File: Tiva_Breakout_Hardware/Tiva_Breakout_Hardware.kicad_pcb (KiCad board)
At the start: 2 copper layers, 139.8 x 79.5 mm, 11 parts, among them U1 TM4C129E_Launchpad

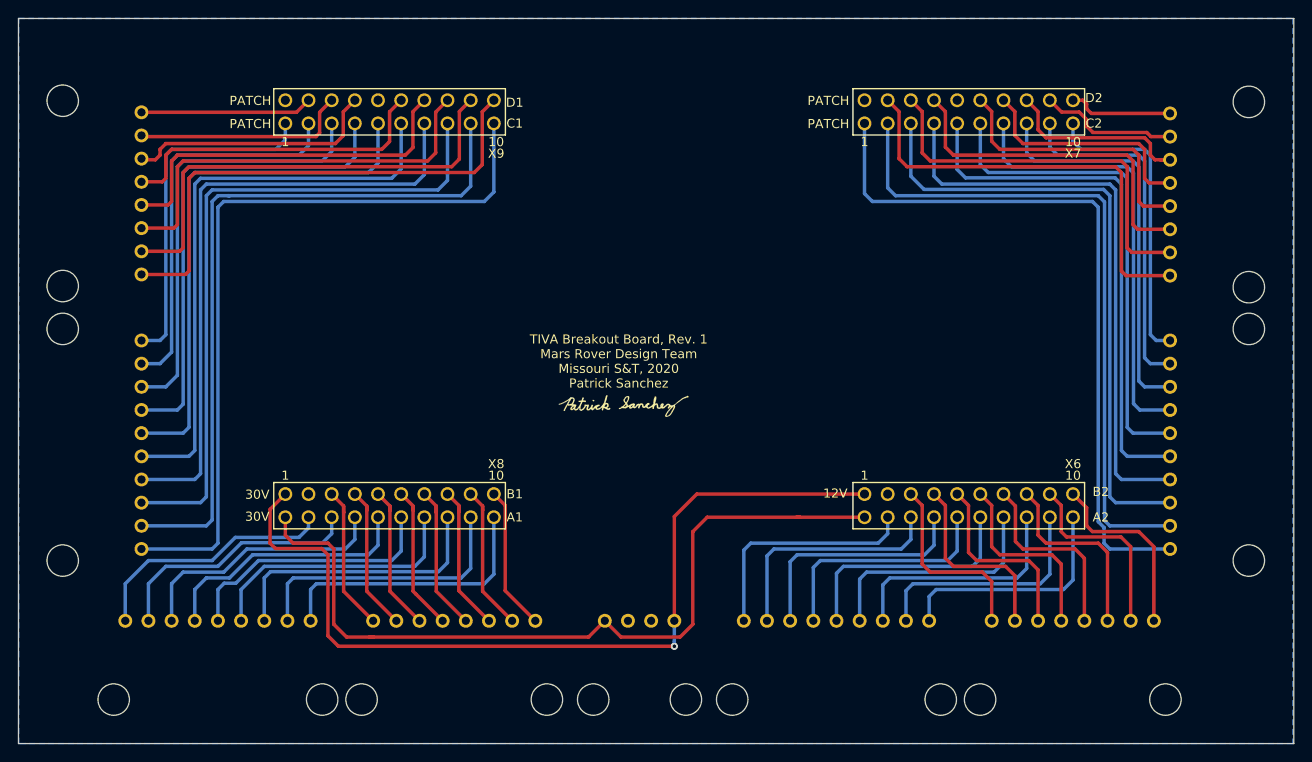
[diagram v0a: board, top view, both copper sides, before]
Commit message: renamed board folder to match standards
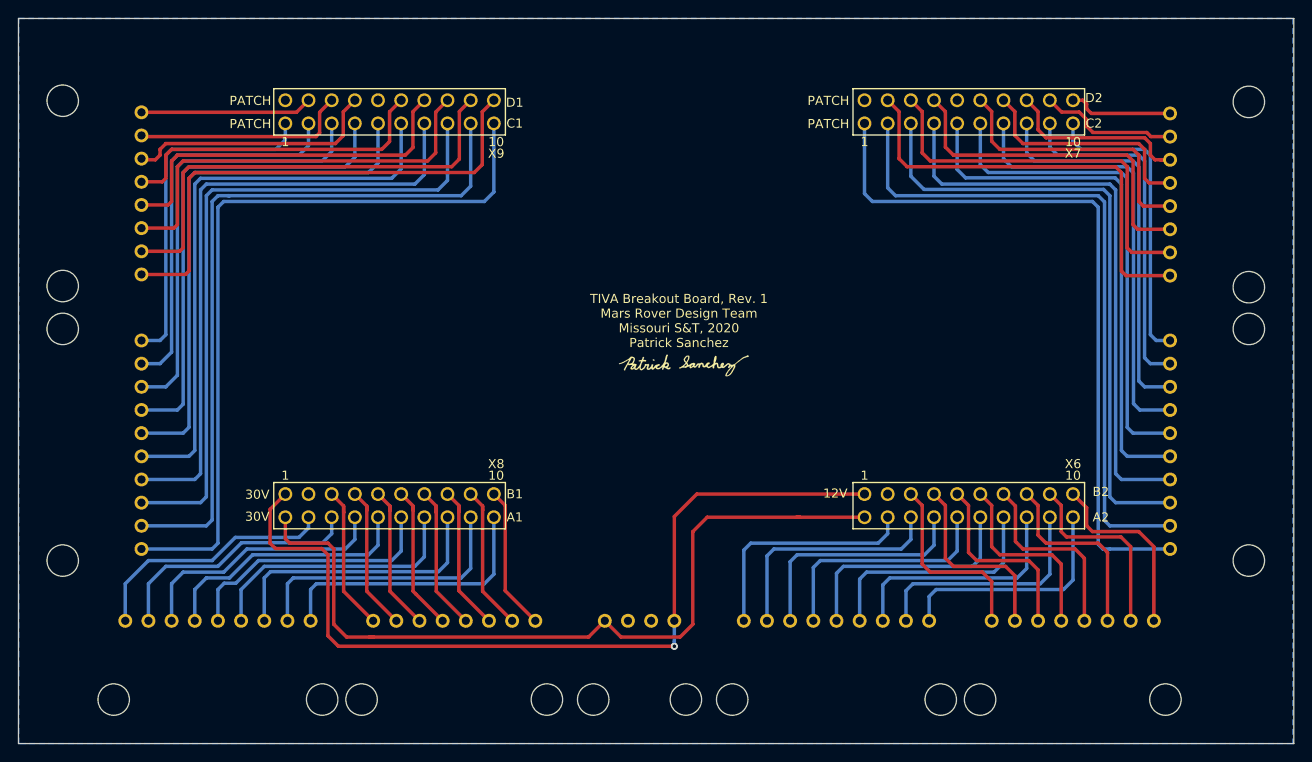
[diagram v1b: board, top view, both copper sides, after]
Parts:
- moved G*** 7.96 mm to (145.0, 90.3)
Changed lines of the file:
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@@
     (thickness 1.6)
     (drawings 135)
-    (tracks 488)
+    (tracks 487)
     (zones 0)
     (modules 11)
@@
   (page A4)
   (layers
-    (0 F.Cu signal)
+    (0 F.Cu signal hide)
     (31 B.Cu signal)
     (32 B.Adhes user)
@@
   )
   (setup
-    (last_trace_width 0.25)
+    (last_trace_width 0.381)
     (user_trace_width 0.254)
     (user_trace_width 0.381)
@@
   )
   (module MRDT_Silkscreens:z_sig_Patrick_Sanchez_15mmx5mm (layer F.Cu)
-    (at 138.43 94.742)
+    (at 145.034 90.297)
     (fp_text reference G*** (at 0 0) (layer F.SilkS) hide
       (effects (font (size 1.524 1.524) (thickness 0.3)))
@@
     )
   )
-  (gr_text "TIVA Breakout Board, Rev. 1\nMars Rover Design Team\nMissouri S&T, 2020\nPatrick Sanchez" (at 137.922 89.916) (layer F.SilkS)
+  (gr_text "TIVA Breakout Board, Rev. 1\nMars Rover Design Team\nMissouri S&T, 2020\nPatrick Sanchez" (at 144.526 85.471) (layer F.SilkS)
     (effects (font (size 1 1) (thickness 0.15)))
   )
@@
   (segment (start 144.018 120.904) (end 144.018 121.158) (width 0.381) (layer B.Cu) (net 1))
   (segment (start 144.018 121.158) (end 144.018 121.158) (width 0.381) (layer B.Cu) (net 1))
-  (via (at 144.018 121.158) (size 0.8) (drill 0.4) (layers F.Cu B.Cu) (net 1) (status 1000000))
+  (via (at 144.018 121.158) (size 0.8) (drill 0.4) (layers F.Cu B.Cu) (net 1))
   (segment (start 99.695 106.145002) (end 101.371001 104.469001) (width 0.381) (layer F.Cu) (net 1))
   (segment (start 99.695 109.855) (end 99.695 106.145002) (width 0.381) (layer F.Cu) (net 1))
@@
   (segment (start 146.05 118.745) (end 146.05 108.585) (width 0.381) (layer F.Cu) (net 3))
   (segment (start 136.398 118.364) (end 134.62 120.142) (width 0.381) (layer F.Cu) (net 3))
-  (segment (start 108.077 120.142) (end 110.998 120.142) (width 0.381) (layer F.Cu) (net 3))
-  (segment (start 106.68 118.745) (end 108.077 120.142) (width 0.381) (layer F.Cu) (net 3))
   (segment (start 110.998 120.142) (end 110.617 120.142) (width 0.381) (layer F.Cu) (net 3))
   (segment (start 134.62 120.142) (end 110.998 120.142) (width 0.381) (layer F.Cu) (net 3))
-  (segment (start 101.371001 107.009001) (end 101.371001 108.991001) (width 0.381) (layer F.Cu) (net 3))
-  (segment (start 101.371001 108.991001) (end 102.235 109.855) (width 0.381) (layer F.Cu) (net 3))
+  (segment (start 101.371001 109.372001) (end 101.854 109.855) (width 0.381) (layer F.Cu) (net 3))
+  (segment (start 101.371001 107.009001) (end 101.371001 109.372001) (width 0.381) (layer F.Cu) (net 3))
+  (segment (start 101.854 109.855) (end 106.045 109.855) (width 0.381) (layer F.Cu) (net 3))
+  (segment (start 108.077 120.142) (end 110.998 120.142) (width 0.381) (layer F.Cu) (net 3))
   (segment (start 106.68 110.49) (end 106.68 118.745) (width 0.381) (layer F.Cu) (net 3))
-  (segment (start 102.235 109.855) (end 106.045 109.855) (width 0.381) (layer F.Cu) (net 3))
   (segment (start 106.045 109.855) (end 106.68 110.49) (width 0.381) (layer F.Cu) (net 3))
+  (segment (start 106.68 118.745) (end 108.077 120.142) (width 0.381) (layer F.Cu) (net 3))
   (segment (start 103.911001 108.178999) (end 103.911001 107.009001) (width 0.381) (layer B.Cu) (net 4))
   (segment (start 93.345 111.76) (end 95.885 109.22) (width 0.381) (layer B.Cu) (net 4))
@@
   (segment (start 167.411001 63.829001) (end 167.411001 70.891001) (width 0.381) (layer B.Cu) (net 56))
   (segment (start 191.18899 107.36899) (end 191.77 107.95) (width 0.381) (layer B.Cu) (net 56))
-  (segment (start 164.871001 71.526001) (end 164.871001 63.829001) (width 0.381) (layer B.Cu) (net 57))
-  (segment (start 165.735 72.39) (end 164.871001 71.526001) (width 0.381) (layer B.Cu) (net 57))
-  (segment (start 191.135 108.136672) (end 190.5 107.501672) (width 0.381) (layer B.Cu) (net 57))
-  (segment (start 190.5 107.501672) (end 190.5 73.025) (width 0.381) (layer B.Cu) (net 57))
-  (segment (start 190.5 73.025) (end 189.865 72.39) (width 0.381) (layer B.Cu) (net 57))
-  (segment (start 189.865 72.39) (end 165.735 72.39) (width 0.381) (layer B.Cu) (net 57))
-  (segment (start 191.135 109.855) (end 191.77 110.49) (width 0.381) (layer B.Cu) (net 57))
-  (segment (start 198.374 110.49) (end 191.77 110.49) (width 0.381) (layer B.Cu) (net 57))
-  (segment (start 191.135 109.855) (end 191.135 108.136672) (width 0.381) (layer B.Cu) (net 57))
+  (segment (start 191.77 110.49) (end 198.374 110.49) (width 0.381) (layer B.Cu) (net 57))
+  (segment (start 164.871001 71.526001) (end 165.735 72.39) (width 0.381) (layer B.Cu) (net 57))
+  (segment (start 164.871001 63.829001) (end 164.871001 71.526001) (width 0.381) (layer B.Cu) (net 57))
+  (segment (start 165.735 72.39) (end 189.865 72.39) (width 0.381) (layer B.Cu) (net 57))
+  (segment (start 189.865 72.39) (end 190.5 73.025) (width 0.381) (layer B.Cu) (net 57))
+  (segment (start 190.5 73.025) (end 190.5 109.982) (width 0.381) (layer B.Cu) (net 57))
+  (segment (start 191.008 110.49) (end 191.77 110.49) (width 0.381) (layer B.Cu) (net 57))
+  (segment (start 190.5 109.982) (end 191.008 110.49) (width 0.381) (layer B.Cu) (net 57))
   (segment (start 124.231001 61.289001) (end 122.9614 62.558602) (width 0.381) (layer F.Cu) (net 58))
   (segment (start 85.598 80.391) (end 90.424 80.391) (width 0.381) (layer F.Cu) (net 58))
